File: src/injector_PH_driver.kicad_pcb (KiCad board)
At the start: 2 copper layers, 126.5 x 52 mm, 59 parts, among them P1 WJ128V-5.0-2P, P2 WJ128V-5.0-2P, P3 WJ128V-5.0-2P, P4 WJ128V-5.0-2P, P5 WJ128V-5.0-2P, P6 WJ128V-5.0-2P, P7 WJ128V-5.0-2P, Q1 BC547B, Q2 IRFZ44NPBF, Q5 BC547B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

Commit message: Added: rough outline
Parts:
- removed C3, C9: c=10u, Capacitor_THT:C_Radial_D5.0mm_H5.0mm_P2.00mm
- removed D18, D19, D20, D21, D26, D27, D28, D29: 1N4007RLG, EasyEDA:DO-41_BD2.4-L4.7-P8.70-D0.9-RD
- removed P1, P2, P3: WJ128V-5.0-2P, EasyEDA:CONN-TH_2P-P5.00_WJ128V-5.0-2P
- removed R12, R13, R3, R4: r=1k, EasyEDA:RES-TH_BD4.2-L12.0-P16.00-D0.8
- removed R14, R20: r=10k, EasyEDA:RES-TH_BD4.2-L12.0-P16.00-D0.8
- removed R15, R21: r=2.2k, EasyEDA:RES-TH_BD4.2-L12.0-P16.00-D0.8
- removed R16, R22: MOF3WS-2.2Ω±5%T, EasyEDA:RES-TH_BD6.0-L17.5-P21.50-D0.7
- removed U1, U3: SQP5W-10Ω±5%-9P, EasyEDA:RES-TH_L22.0-W10.0-P26.00-D1.0
- D1, D14, D2, D3, D4: value 1.5KE18A_C132974 -> DF2S6P2FU,H3F; footprint EasyEDA:DO-201_BD5.3-L9.5-P13.50-D1.4-FD -> EasyEDA:USC_L1.7-W1.3-LS2.5-R-RD
- D16, D17, D6, D7: value 1N4007RLG -> MRA4007T3G; footprint EasyEDA:DO-41_BD2.4-L4.7-P8.70-D0.9-RD -> EasyEDA:SMA_L4.3-W2.6-LS5.2-RD
- OSC1, OSC3: footprint EasyEDA:PDIP-8_L9.3-W6.4-P2.54-LS7.9-BL-1 -> EasyEDA:SOIC-8_L4.9-W3.9-P1.27-LS6.0-BL
- Q1, Q5: value BC547B -> BC847BT-7-F; footprint EasyEDA:TO-92-3_L4.9-W3.7-P1.27-L -> EasyEDA:SOT-523-3_L1.6-W0.8-P1.00-LS1.6-BR
- Q2, Q6: value IRFZ44NPBF -> IRFZ44NSTRLPBF; footprint EasyEDA:TO-220-3_L10.0-W4.5-P2.54-L -> EasyEDA:TO-263-2_L10.0-W9.1-P5.08-LS15.2-TL
- R1, R10: footprint EasyEDA:RES-TH_BD4.2-L12.0-P16.00-D0.8 -> EasyEDA:R0603
- R11, R2: value r=1k -> r=10k; footprint EasyEDA:RES-TH_BD4.2-L12.0-P16.00-D0.8 -> EasyEDA:R0603
- moved H1 126.6 mm to (91.5, 27.5), turned to 0 degrees
- moved P6 122.6 mm to (93.5, 67.0), turned to -90 degrees
- moved P7 122.3 mm to (93.5, 57.0), turned to -90 degrees
- moved H2 115.6 mm to (128.5, 27.5)
- moved G*** 115.2 mm to (225.5, 33.5)
- moved P4 107.5 mm to (93.5, 37.0), turned to -90 degrees
- moved D16 103.4 mm to (103.0, 39.0)
- moved D6 99.9 mm to (103.8, 72.0), turned to 0 degrees
- moved D17 97.5 mm to (111.0, 39.0), turned to 0 degrees
- moved D7 93.8 mm to (111.4, 72.0)
- moved P5 92.7 mm to (93.5, 47.0), turned to -90 degrees
- moved Q2 88.2 mm to (109.0, 64.0)
- moved D5 87.2 mm to (115.2, 76.4), turned to 0 degrees
- moved D15 84.1 mm to (115.5, 33.0)
- moved C1 83.3 mm to (123.4, 55.2)
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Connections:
- OSC1 pad 2: Net-(OSC1-INPUT) -> Net-(OSC1-IN)
- OSC3 pad 2: Net-(OSC3-INPUT) -> Net-(OSC3-IN)
- Q1 pad 1: Net-(OSC1-INPUT) -> Net-(Q1-B)
- Q1 pad 2: Net-(Q1-B) -> GND
- Q1 pad 3: GND -> Net-(OSC1-IN)
- Q2 pad 3: Net-(Q2-S) -> GND
- Q5 pad 1: Net-(OSC3-INPUT) -> Net-(Q5-B)
- Q5 pad 2: Net-(Q5-B) -> GND
- Q5 pad 3: GND -> Net-(OSC3-IN)
- Q6 pad 3: Net-(Q6-S) -> GND
- R1 pad 1: /Drv1 -> Net-(Q1-B)
- R1 pad 2: Net-(Q1-B) -> /Drv1
- R10 pad 1: /Drv2 -> Net-(Q5-B)
- R10 pad 2: Net-(Q5-B) -> /Drv2
- R11 pad 2: Net-(OSC3-INPUT) -> Net-(OSC3-IN)
- R2 pad 2: Net-(OSC1-INPUT) -> Net-(OSC1-IN)
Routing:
- net /injector_sense2/dummy_output_ttl: track 84.0 -> 0.00 mm
- net /Inj2-: track 63.0 -> 0.00 mm
- net /injector_sense1/dummy_output_ttl: track 56.6 -> 0.00 mm
- net /injector_sense2/HIGH: track 52.9 -> 0.00 mm
- net /Inj1-: track 40.5 -> 0.00 mm
- net /injector_sense1/dummy-: track 37.9 -> 0.00 mm
- net /driver1/mosfet_power: track 33.3 -> 0.00 mm
- net /injector_sense2/dummy-: track 24.1 -> 0.00 mm
- net /Drv2: track 56.6 -> 33.6 mm
- net /driver2/mosfet_power: track 25.4 -> 2.49 mm
- net Net-(OSC1-INPUT): track 21.7 -> 0.00 mm
- net Net-(Q2-S): track 21.1 -> 0.00 mm
- net /injector_sense1/HIGH: track 20.7 -> 0.00 mm
- net Net-(OSC3-INPUT): track 18.4 -> 0.00 mm
- net Net-(R22-Pad2): track 12.3 -> 0.00 mm
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- added copper zone on F.Cu, net /Inj2-
- added copper zone on F.Cu, net /driver2/mosfet_power
- added copper zone on F.Cu, net GND
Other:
- board size 126.5 x 52 mm -> 45 x 57 mm
- board text removed: "1"
- board text removed: "12V"
- board text removed: "2"
- board text removed: "Drv1"
- board text removed: "Drv2"
- board text removed: "Dummy1+"
- board text removed: "Dummy1-"
- board text removed: "Dummy2+"
- board text removed: "Dummy2-"
- board text removed: "GND"
- board text removed: "Inj1+"
- board text removed: "Inj1-"
- board text removed: "Inj2+"
- board text removed: "Inj2-"
- board text removed: "sense OUT"

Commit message: Finished routing
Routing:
- net Net-(OSC1-IN): track 0.00 -> 4.48 mm
- net /Drv1: track 45.9 -> 48.2 mm
- net GND: track 5.38 -> 6.58 mm
- added copper zone on B.Cu, net /Inj1-
- added copper zone on F.Cu, net /Inj1-
- added copper zone on B.Cu, net /Inj2-
- added copper zone on F.Cu, net /driver1/mosfet_power

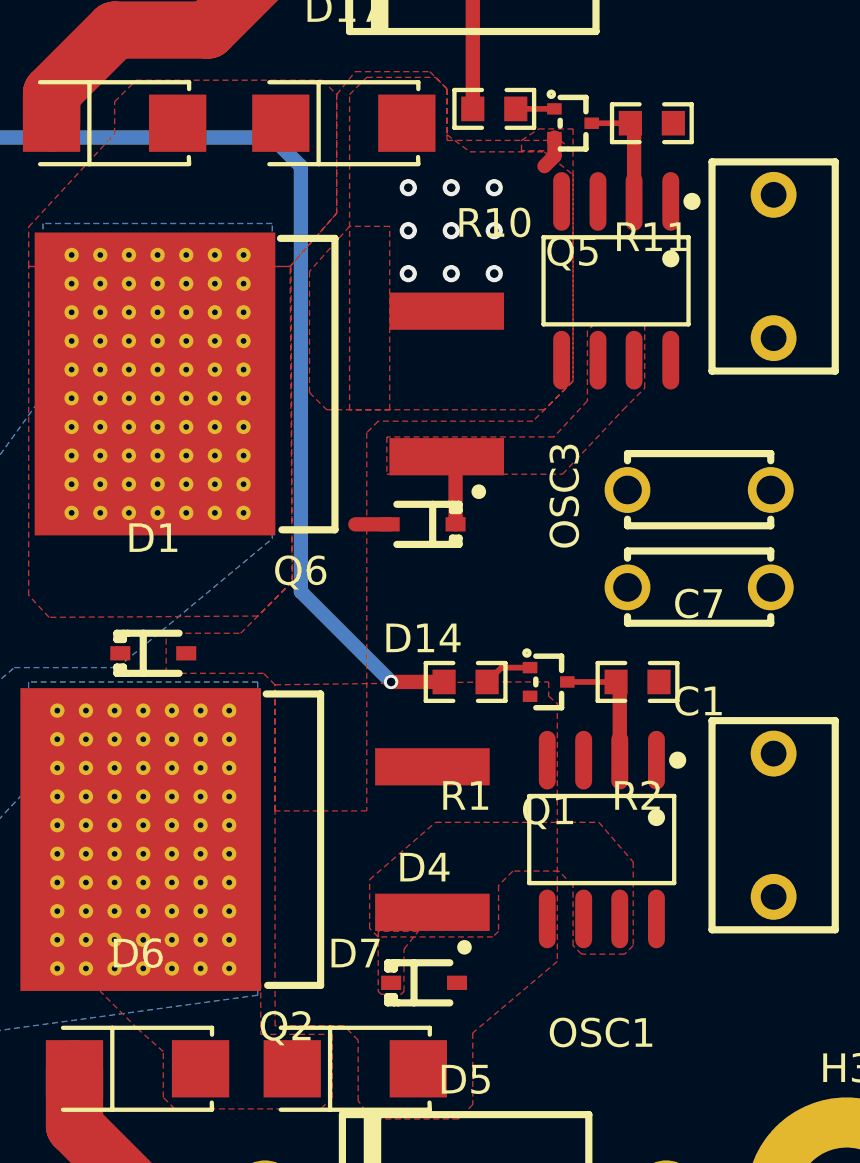
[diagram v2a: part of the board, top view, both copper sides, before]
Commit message: Updated: ground plane couplling vias
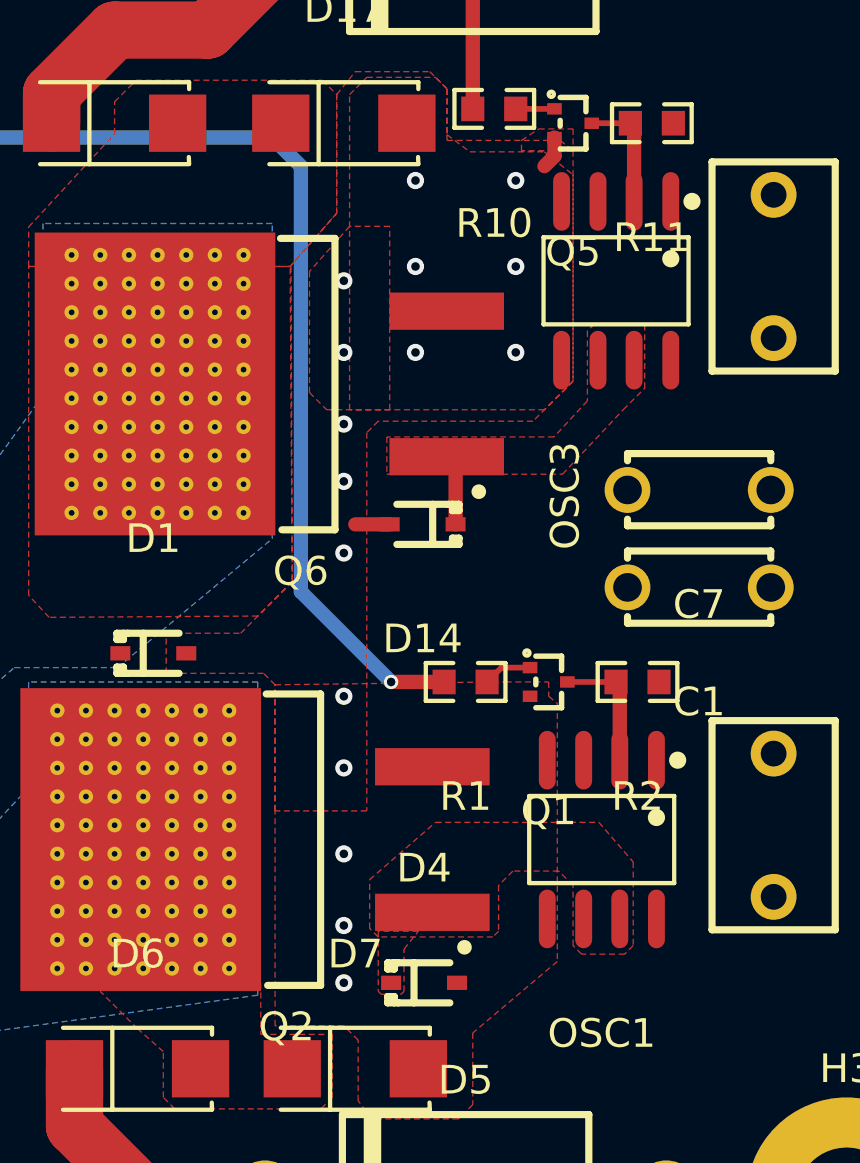
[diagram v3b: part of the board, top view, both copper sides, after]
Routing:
- net GND: vias 12 -> 19
